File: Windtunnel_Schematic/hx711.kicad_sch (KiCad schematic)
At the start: 0 parts

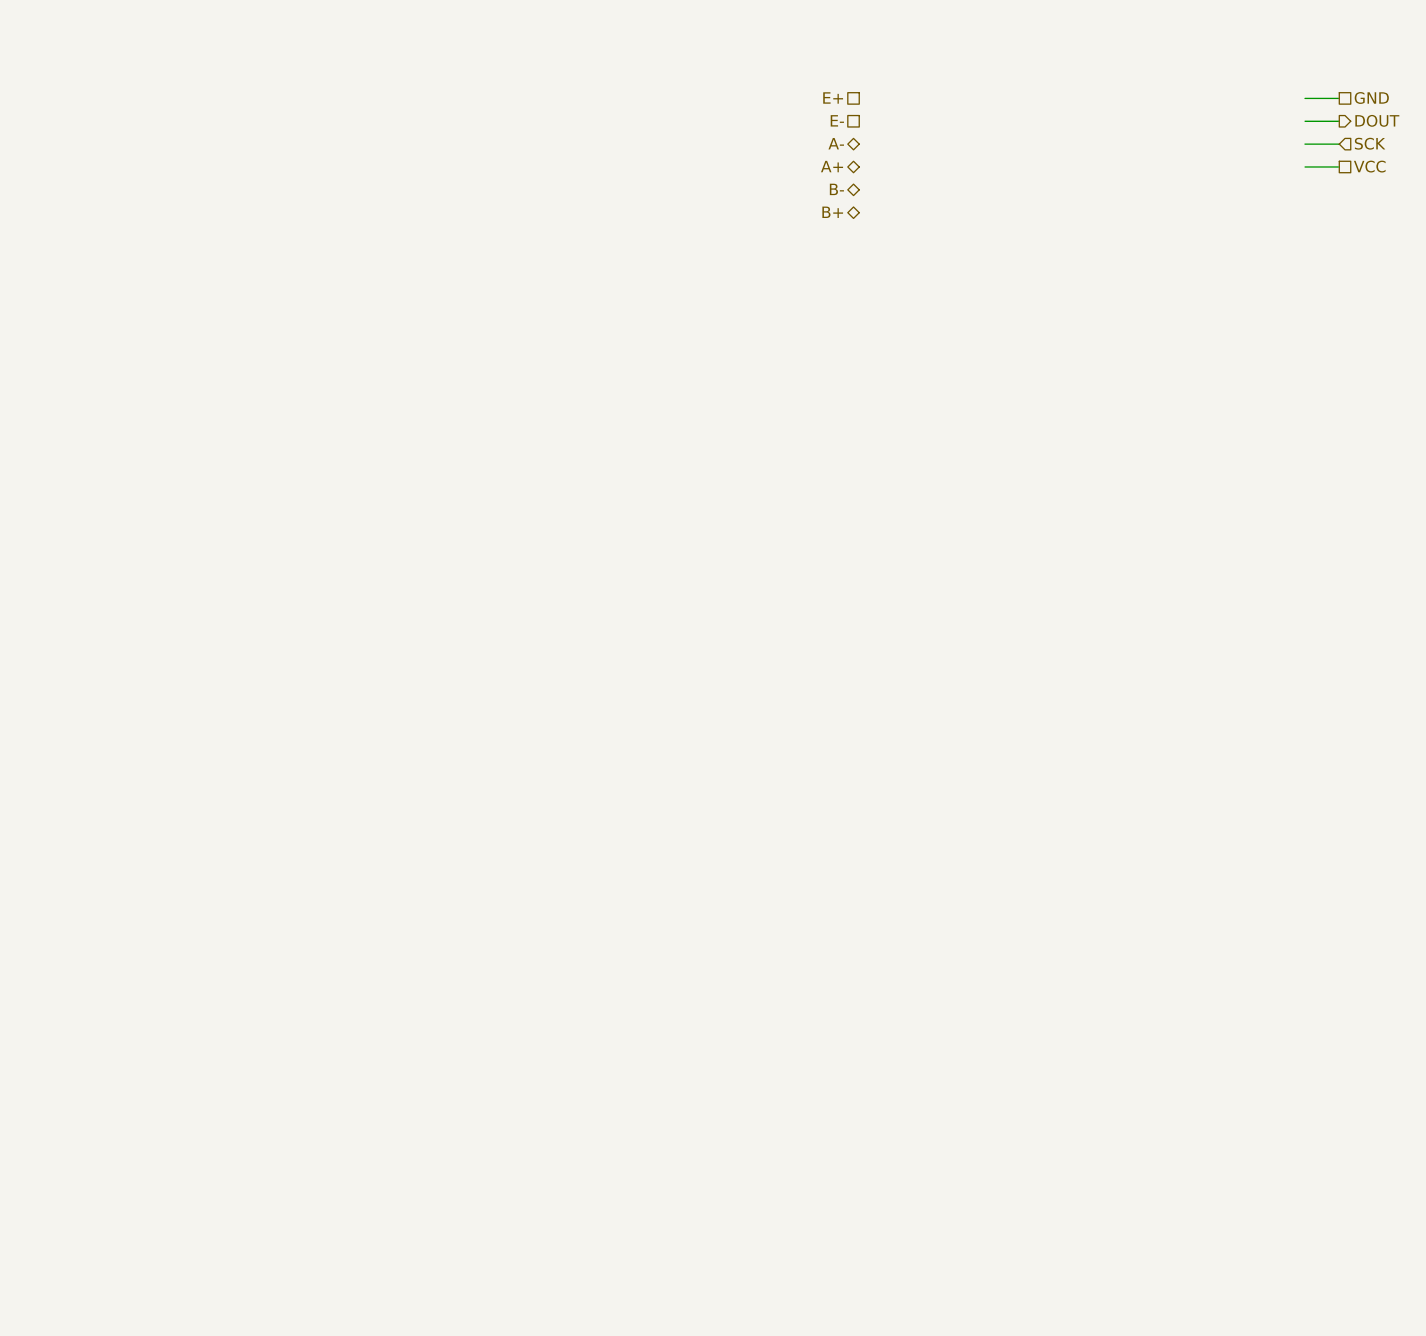
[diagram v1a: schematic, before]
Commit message: Schematic to 0.3.0 Nearly finished Trying to mill it tomorrow
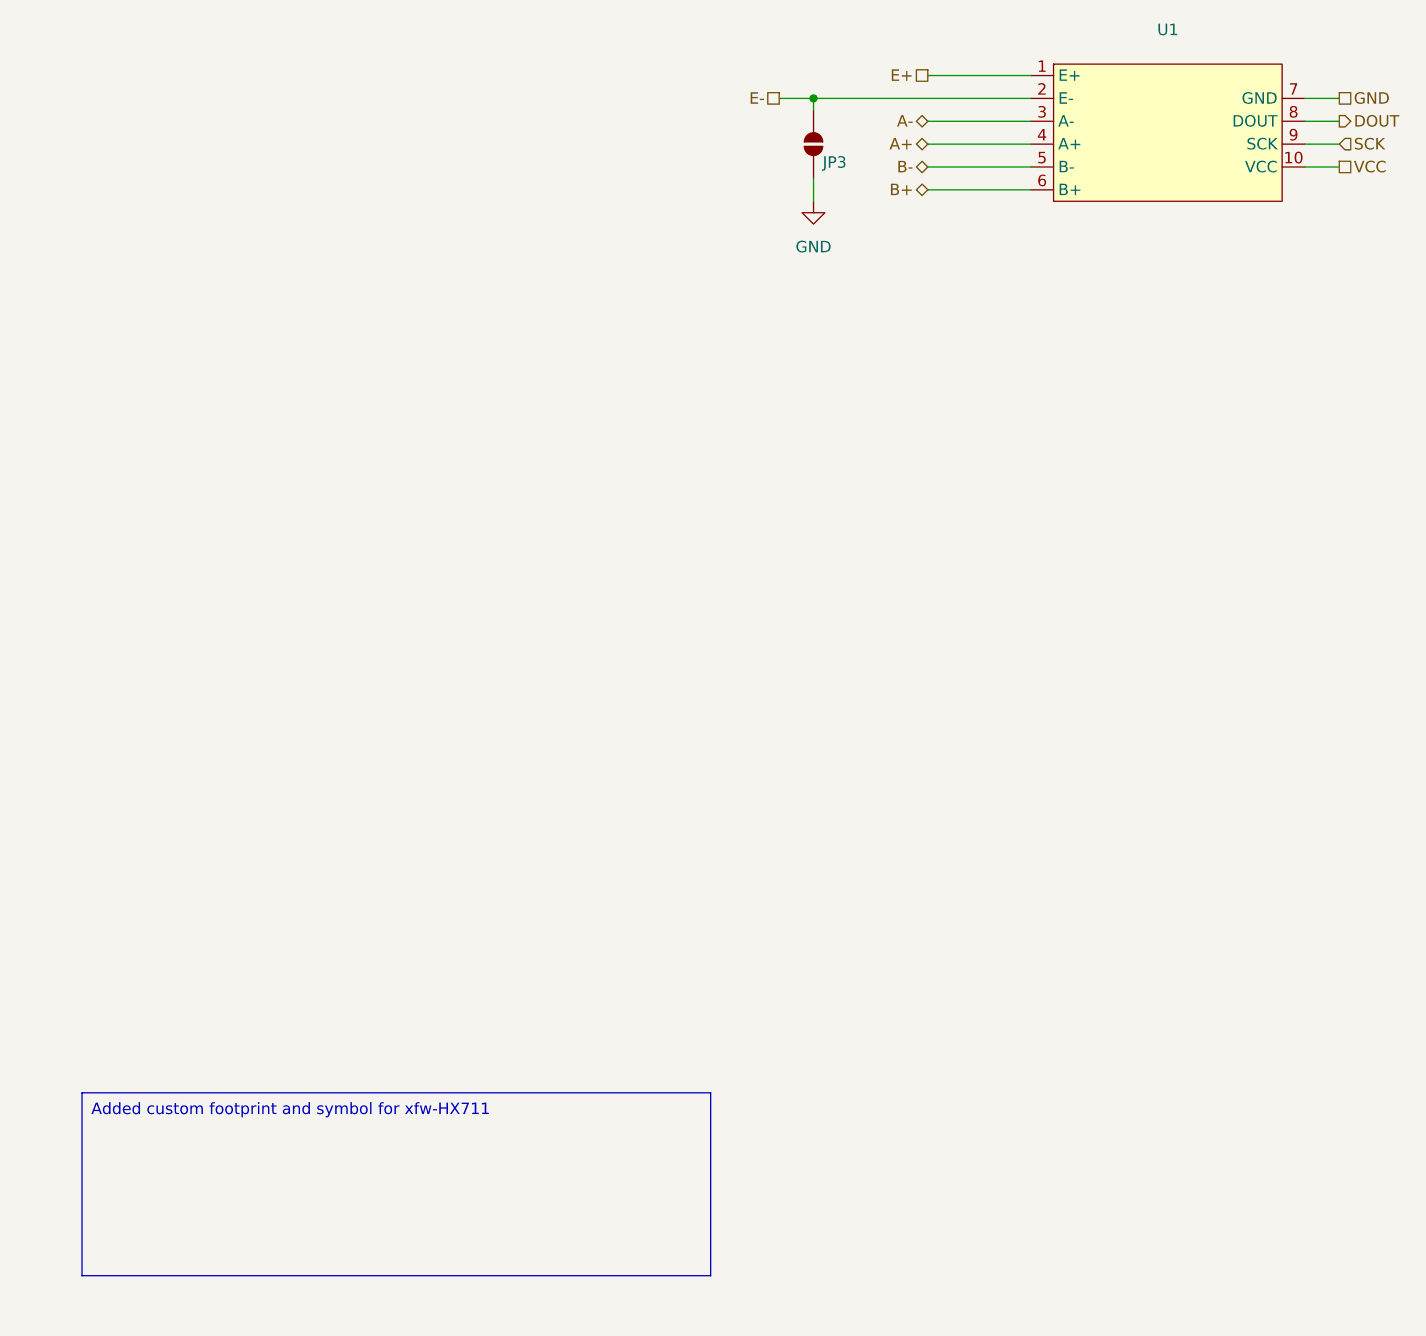
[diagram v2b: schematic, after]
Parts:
- added JP3: SolderJumper_2_Open, Jumper:SolderJumper-2_P1.3mm_Open_TrianglePad1.0x1.5mm, symbol Jumper:SolderJumper_2_Open
- added U1: ~, Library:xfw_hx711, symbol Windtunnel:xfw_hx711
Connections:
- net A+: now also U1.4 (A+)
- net A-: now also U1.3 (A-)
- net B+: now also U1.6 (B+)
- net B-: now also U1.5 (B-)
- net DOUT: now also U1.8 (DOUT)
- net E+: now also U1.1 (E+)
- net E-: now also JP3.2 (B), U1.2 (E-)
- net GND: now also JP3.1 (A), U1.7 (GND)
- net SCK: now also U1.9 (SCK)
- net VCC: now also U1.10 (VCC)

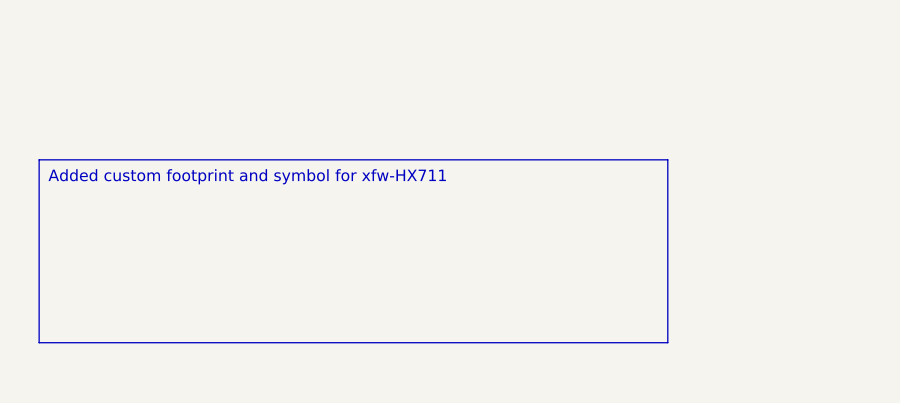
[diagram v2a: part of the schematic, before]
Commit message: Schematic: First version is done and working TODO: Add labling to pcb Add comments Add changes for next version, but we will not manufacture this one
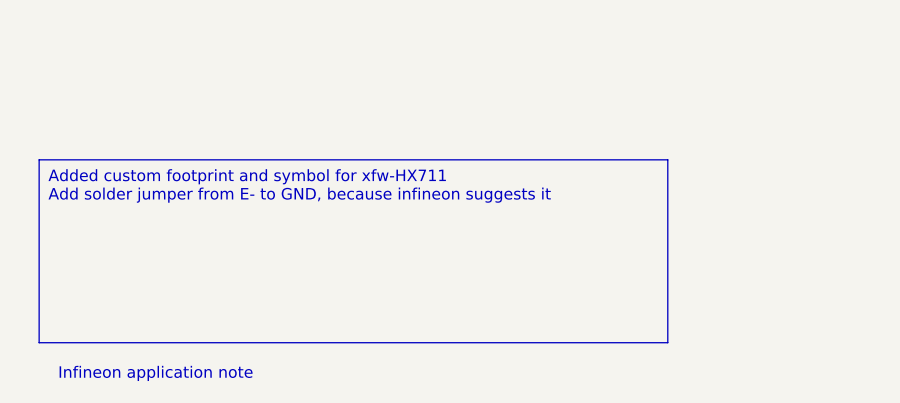
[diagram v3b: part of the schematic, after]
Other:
- note added: "Infineon application note"
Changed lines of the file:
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@@
 		)
 	)
-	(text_box "Added custom footprint and symbol for xfw-HX711"
+	(text_box "Added custom footprint and symbol for xfw-HX711\nAdd solder jumper from E- to GND, because infineon suggests it "
 		(exclude_from_sim no)
 		(at 21.59 168.91 0)
@@
 		)
 	)
+	(text "Infineon application note"
+		(exclude_from_sim no)
+		(at 34.544 192.786 0)
+		(effects
+			(font
+				(size 1.27 1.27)
+			)
+			(href "file://../Docs/Datasheets/HX711_v0_0_B-2.pdf")
+		)
+	)

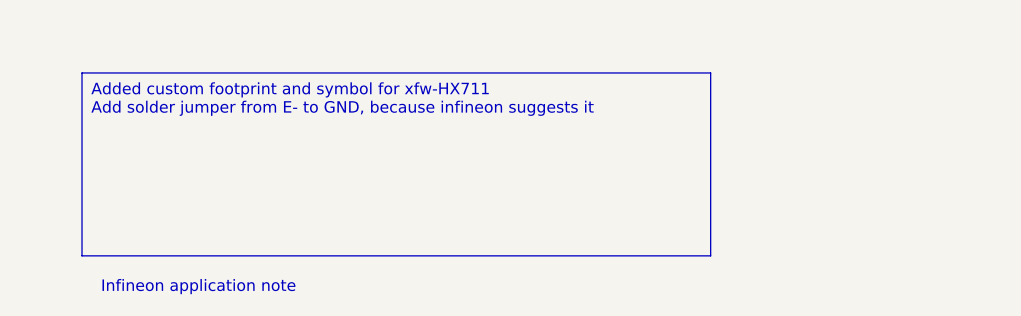
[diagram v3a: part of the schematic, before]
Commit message: Add to docs, schematic and general calculation: ADD prototype data Change Schematic revision to 0.4.0 ADD requirements.txt for each general calculation virtual environment
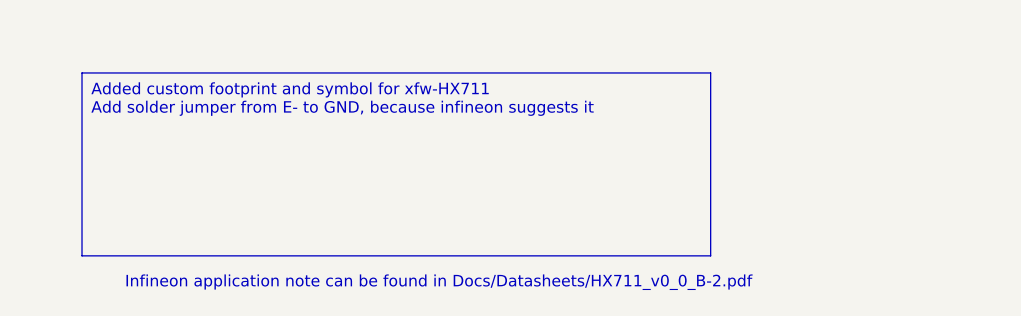
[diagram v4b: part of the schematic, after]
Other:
- note added: "Infineon application note can be found in Docs/Datasheets/HX711_v0_0_B-2.pdf"
- note removed: "Infineon application note"
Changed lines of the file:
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@@
 	(title_block
 		(title "Schematic for wind tunnel measurement system")
-		(rev "0.3.0")
+		(rev "0.4.0")
 		(company "Reykjavik University")
 	)
@@
 		)
 	)
-	(text "Infineon application note"
+	(text "Infineon application note can be found in Docs/Datasheets/HX711_v0_0_B-2.pdf"
 		(exclude_from_sim no)
-		(at 34.544 192.786 0)
+		(at 61.214 192.278 0)
 		(effects
 			(font
 				(size 1.27 1.27)
 			)
-			(href "file://../Docs/Datasheets/HX711_v0_0_B-2.pdf")
 		)
 	)
